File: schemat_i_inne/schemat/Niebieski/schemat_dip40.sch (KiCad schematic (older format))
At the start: 23 parts, among them J1 Hole1, J2 Hole2, J3 Hole3, J4 Hole4, J5 RJ45, SW1 SW_DIP_x01, SW2 Left, SW3 Up, SW4 Down, SW5 Right, SW6 Jump, SW7 Punch, U1 ATmega32A-AU, U2 L7805, U3 WG12864B-STBL, U4 SD_card_reader, Y1 16Mhz

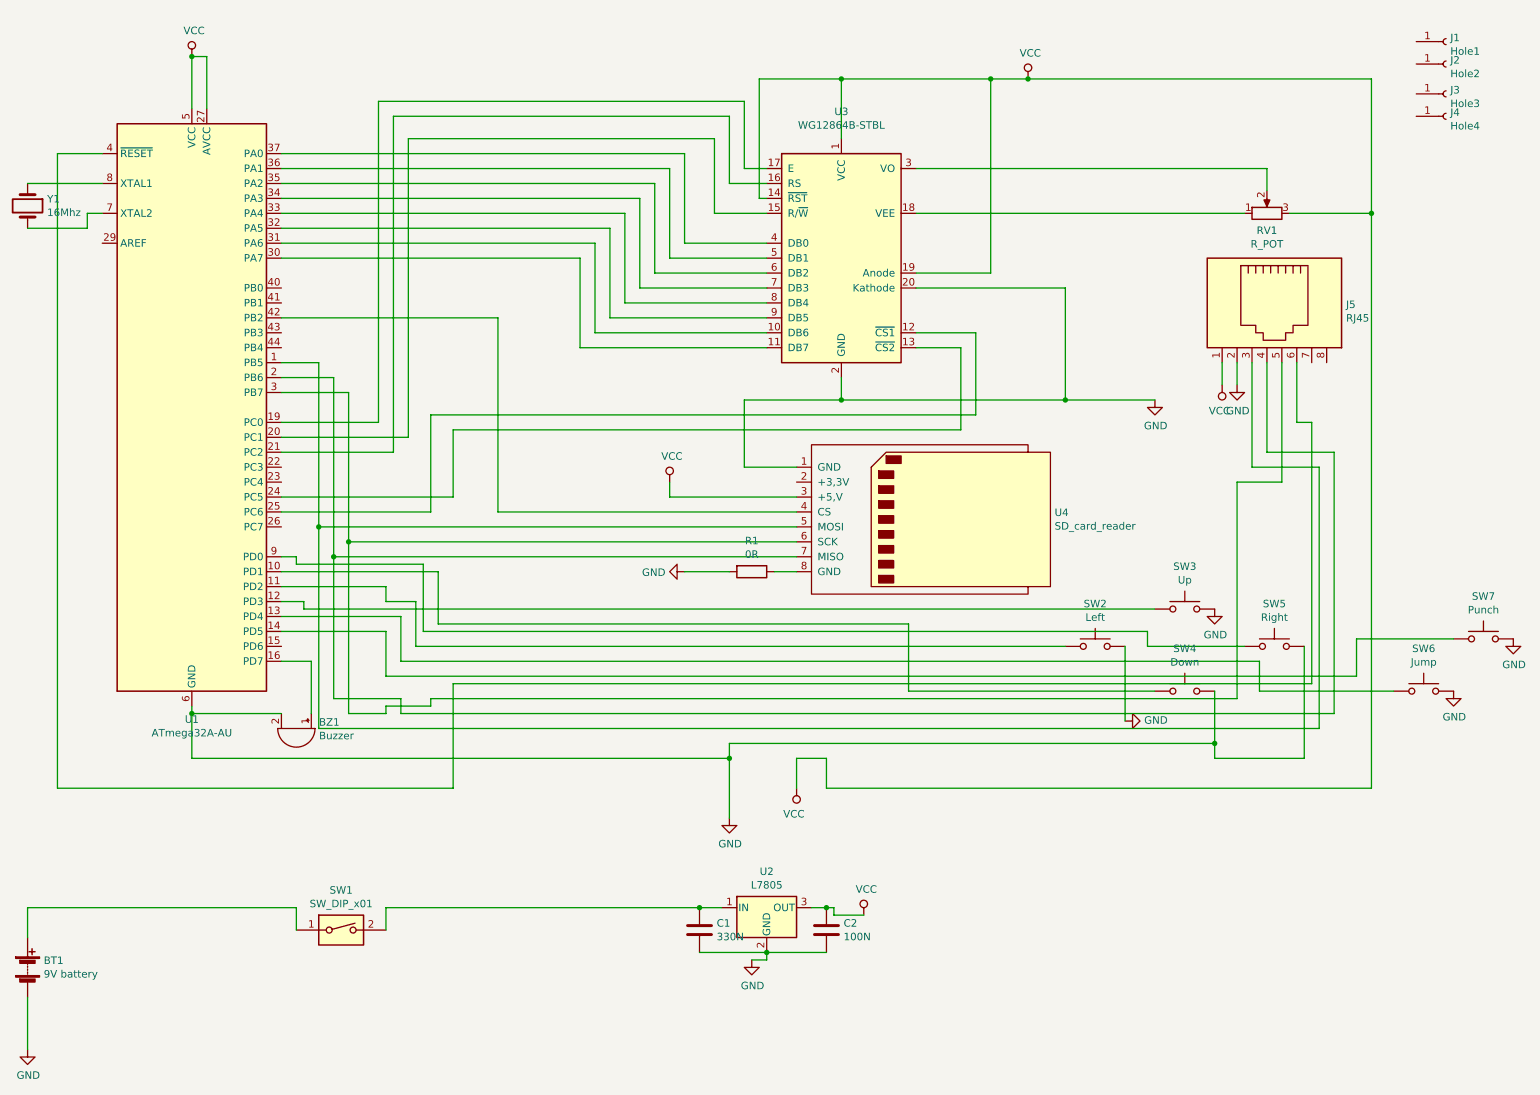
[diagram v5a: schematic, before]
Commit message: Upraszczanie polaczen i poprawianie plytki
Gotowe polaczenia do ekranu
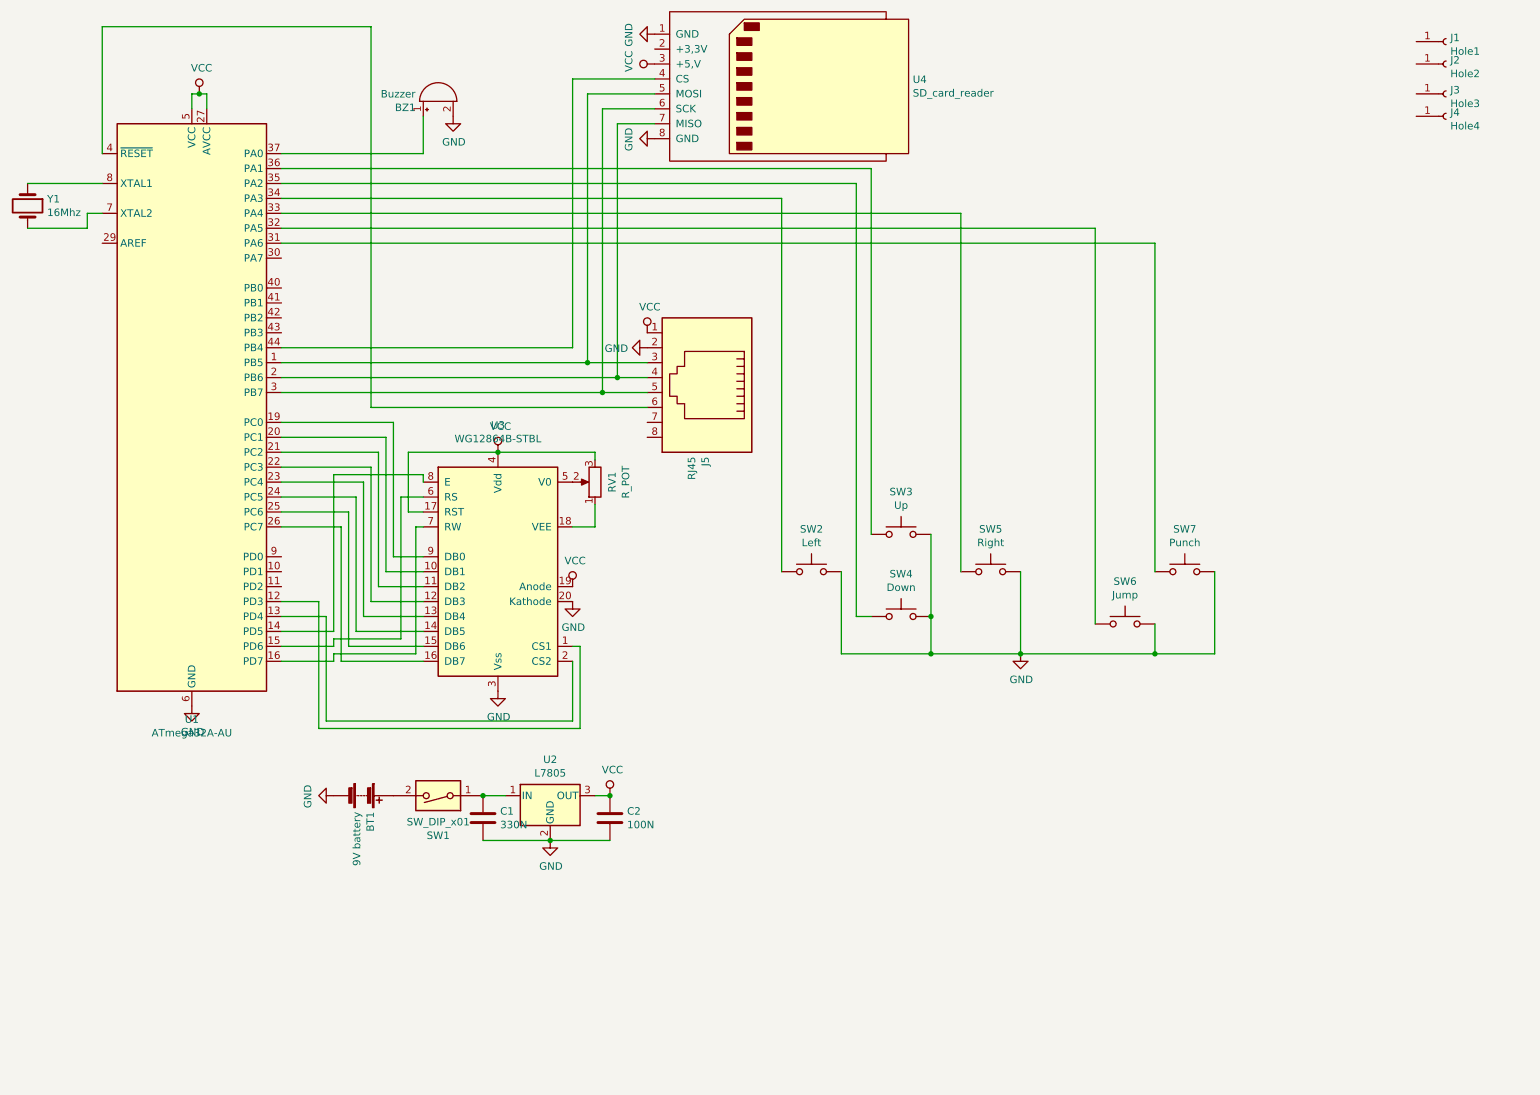
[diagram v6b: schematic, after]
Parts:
- removed R1: 0R, Resistor_THT:R_Axial_DIN0204_L3.6mm_D1.6mm_P2.54mm_Vertical, symbol Device:R
- removed U3: WG12864B-STBL, Blue:WG12864BL, symbol schemat_dip40-rescue:WG12864B-STBL-schemat_dip40-rescue
- added U3: WG12864B-STBL, Blue:WG12864BL, symbol schemat_dip40-rescue:WG12864B-STBL
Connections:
- net GND: now also U4.8 (GND), U3.20 (Kathode), U3.3 (Vss)
- net VCC: now also U3.17 (RST), U3.19 (Anode), U3.4 (Vdd)
- net at U4.4 (CS): now also U1.44 (PB4); no longer U1.42 (PB2)
- net at SW3.1: now also U1.36 (PA1); no longer U1.12 (PD3)
- net at SW4.1: now also U1.35 (PA2); no longer U1.10 (PD1)
- net at SW5.1: now also U1.33 (PA4); no longer U1.9 (PD0)
- net at SW2.1: now also U1.34 (PA3); no longer U1.11 (PD2)
- net at SW6.1: now also U1.32 (PA5); no longer U1.13 (PD4)
- net at SW7.1: now also U1.31 (PA6); no longer U1.14 (PD5)
- net at U1.25 (PC6): now also U3.15 (DB6)
- net at U1.24 (PC5): now also U3.14 (DB5)
- net at U1.20 (PC1): now also U3.10 (DB1)
- net at U1.21 (PC2): now also U3.11 (DB2)
- net at U1.19 (PC0): now also U3.9 (DB0)
- net at RV1.1: now also U3.18 (VEE)
- net at RV1.2: now also U3.5 (V0)
- net at U1.37 (PA0): now also BZ1.1 (-)
- net at U1.15 (PD6): now also U3.6 (RS)
- net at U1.16 (PD7): now also U3.7 (RW); no longer BZ1.1 (-)
- net at U1.22 (PC3): now also U3.12 (DB3)
- net at U1.23 (PC4): now also U3.13 (DB4)
- net at U1.26 (PC7): now also U3.16 (DB7)
- net at C1.1, U2.1 (IN): now also SW1.1; no longer SW1.2
- net at BT1.1 (+): now also SW1.2; no longer SW1.1
- new net: U1.12 (PD3), U3.1 (CS1)
- new net: U1.13 (PD4), U3.2 (CS2)
- new net: U1.14 (PD5), U3.8 (E)
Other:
- moved on the sheet: BT1, BZ1, C1, C2, J5, RV1, SW1, SW2, SW3, SW4, SW5, SW6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

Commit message: Wiele elementow dodanych
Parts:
- added R1: 0R, Resistor_THT:R_Axial_DIN0204_L3.6mm_D1.6mm_P7.62mm_Horizontal, symbol Device:R
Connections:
- net GND: now also R1.2; no longer U3.3 (Vss)
- new net: R1.1, U3.3 (Vss)

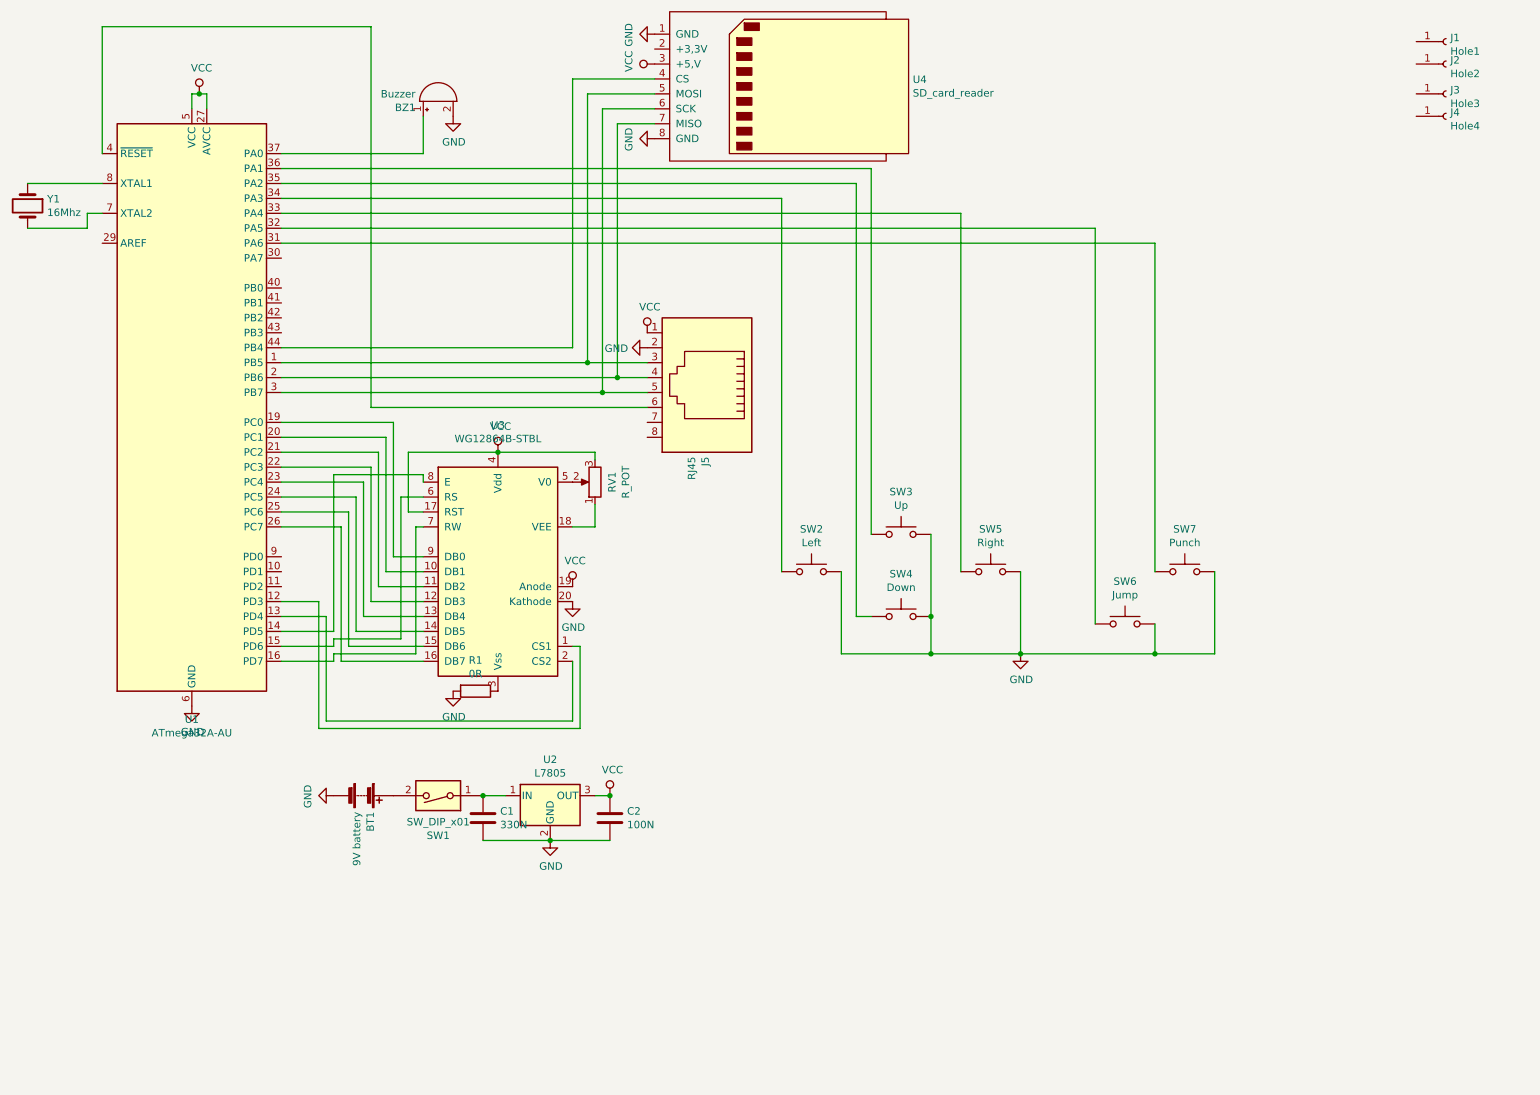
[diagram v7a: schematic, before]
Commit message: Wszystkie polaczenia
Zrealizowano wszystkie polaczenia, wygaldaja okropnie ale sa XD
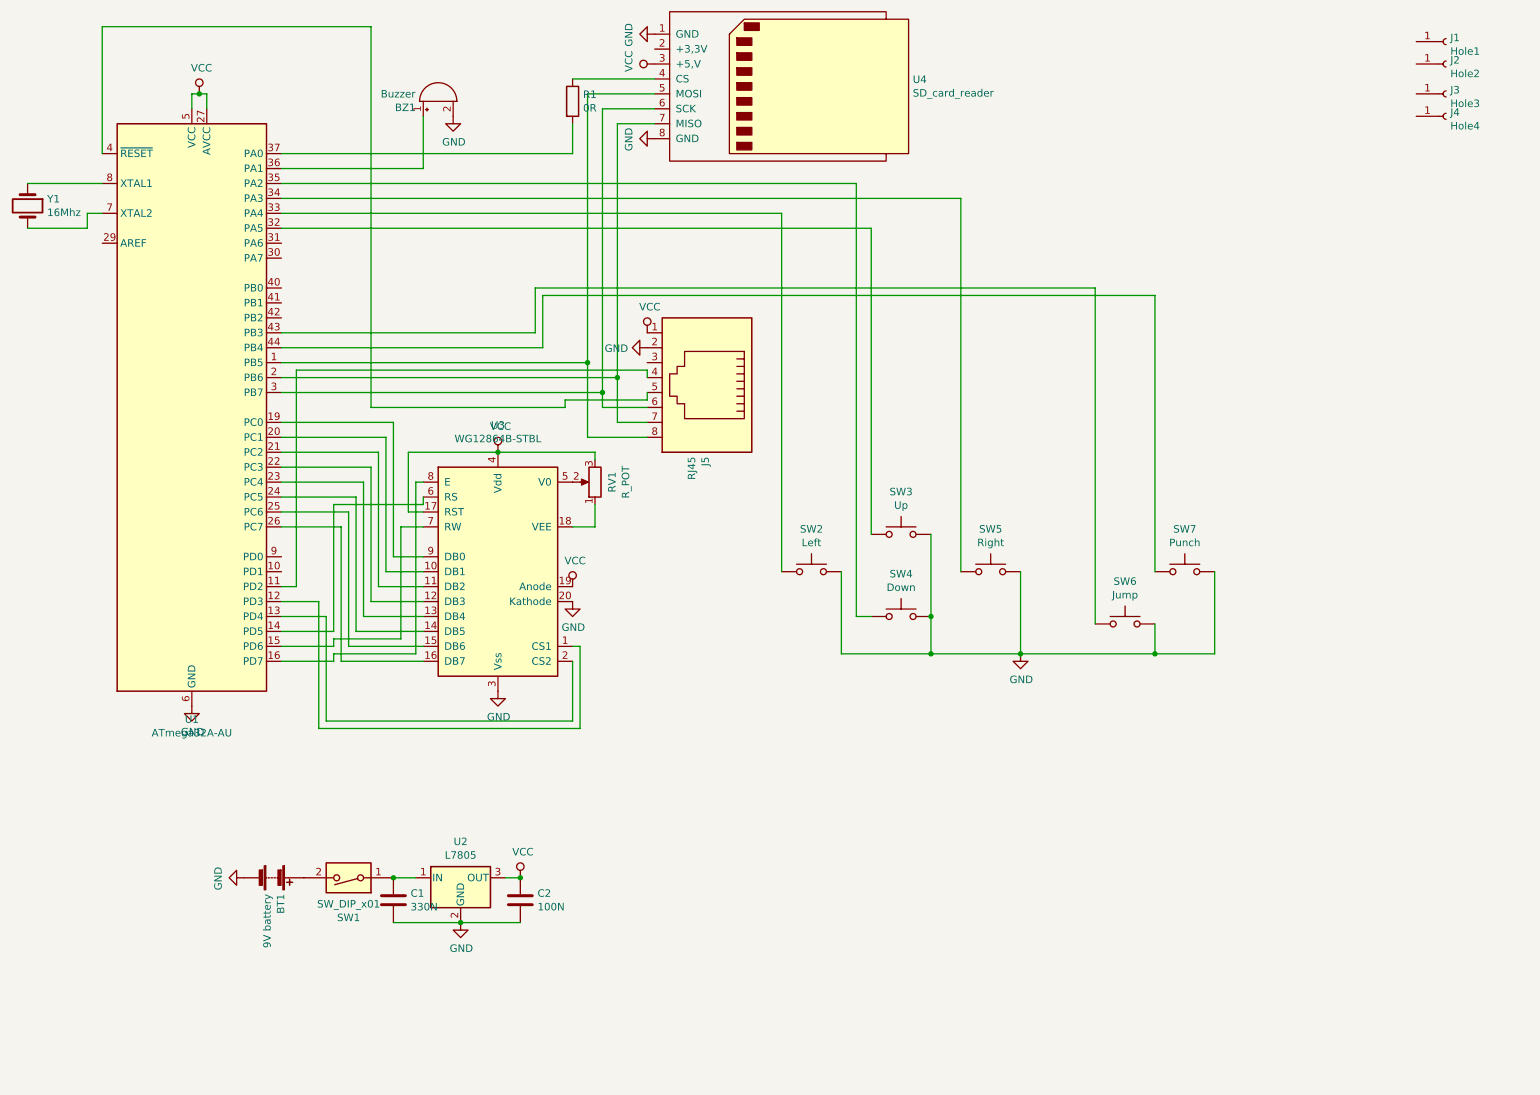
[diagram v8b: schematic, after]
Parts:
- R1: footprint Resistor_THT:R_Axial_DIN0204_L3.6mm_D1.6mm_P7.62mm_Horizontal -> Resistor_THT:R_Axial_DIN0207_L6.3mm_D2.5mm_P10.16mm_Horizontal
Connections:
- net GND: now also U3.3 (Vss); no longer R1.2
- net at U4.4 (CS): now also R1.1; no longer U1.44 (PB4)
- net at U1.1 (PB5), U4.5 (MOSI): now also J5.8; no longer J5.3
- net at U1.3 (PB7), U4.6 (SCK): now also J5.6; no longer J5.5
- net at U1.2 (PB6), U4.7 (MISO): now also J5.7; no longer J5.4
- net at SW3.1: now also U1.32 (PA5); no longer U1.36 (PA1)
- net at SW5.1: now also U1.34 (PA3); no longer U1.33 (PA4)
- net at SW2.1: now also U1.33 (PA4); no longer U1.34 (PA3)
- net at SW6.1: now also U1.43 (PB3); no longer U1.32 (PA5)
- net at SW7.1: now also U1.44 (PB4); no longer U1.31 (PA6)
- net at U1.11 (PD2): now also J5.4
- net at U1.14 (PD5): now also U3.6 (RS); no longer U3.8 (E)
- net at U1.15 (PD6): now also U3.7 (RW); no longer U3.6 (RS)
- net at U1.16 (PD7): now also U3.8 (E); no longer U3.7 (RW)
- net at BZ1.1 (-): now also U1.36 (PA1); no longer U1.37 (PA0)
- net at U1.4 (~RESET): now also J5.5; no longer J5.6
- new net: R1.2, U1.37 (PA0)
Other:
- moved on the sheet: BT1, C1, C2, SW1, U2
